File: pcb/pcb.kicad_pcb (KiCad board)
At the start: 2 copper layers, 129 parts, among them J1 Conn_01x06, J2 SPI_Flash, SW1 Select, SW2 Done, U1 ATmega328P-AU, U2 DessinAfficheur, Y1 16Mhz

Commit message: fix i2c label
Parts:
- J1: value Conn_01x06 -> I2C_Data

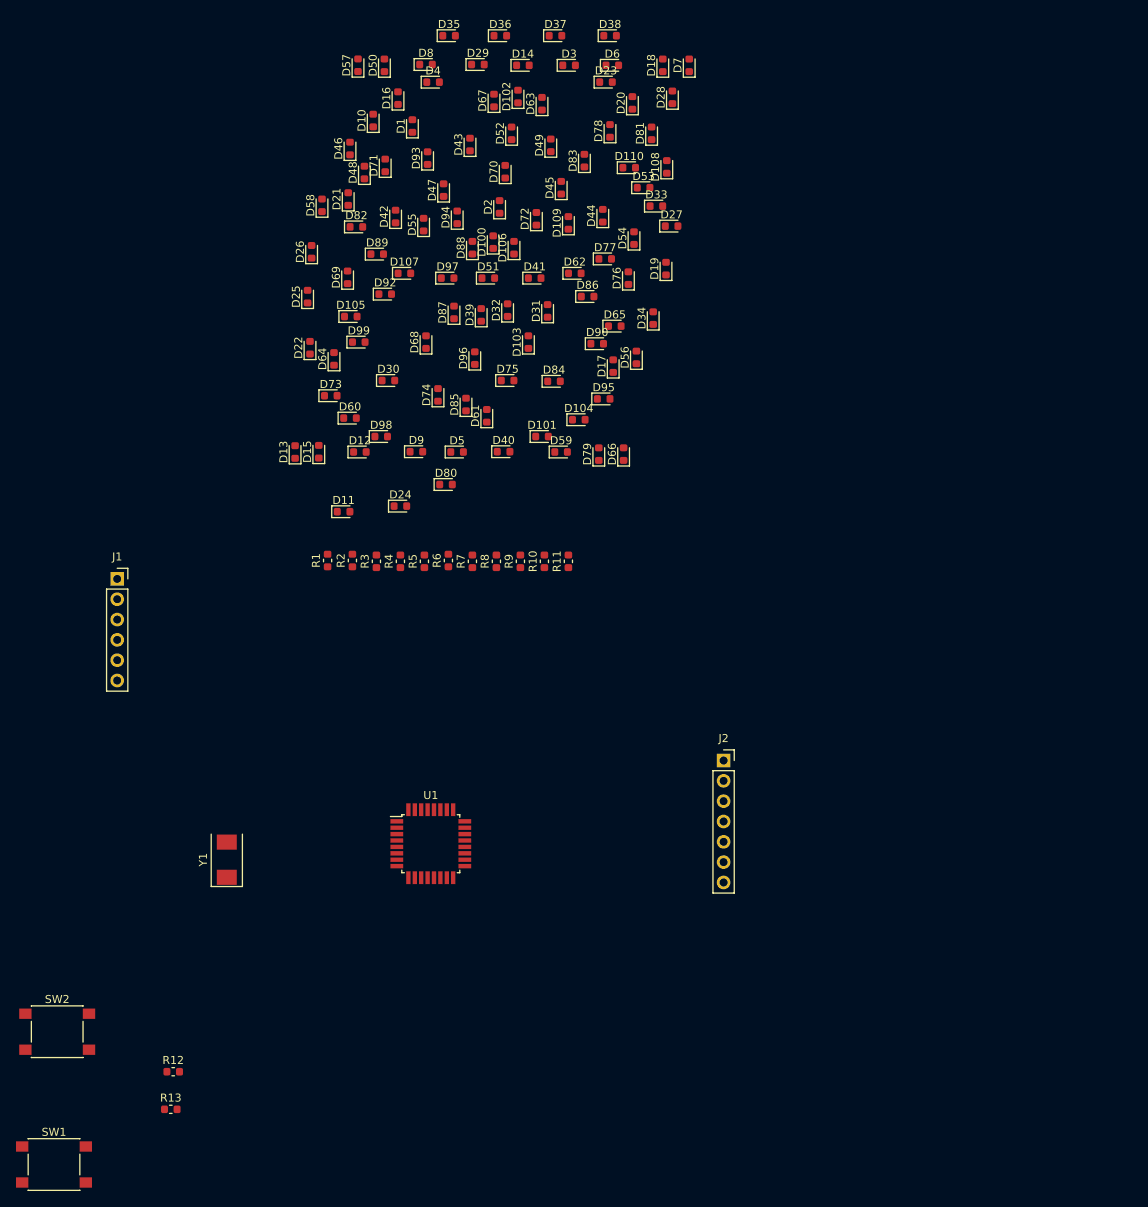
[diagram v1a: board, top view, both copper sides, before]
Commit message: put all components on the board
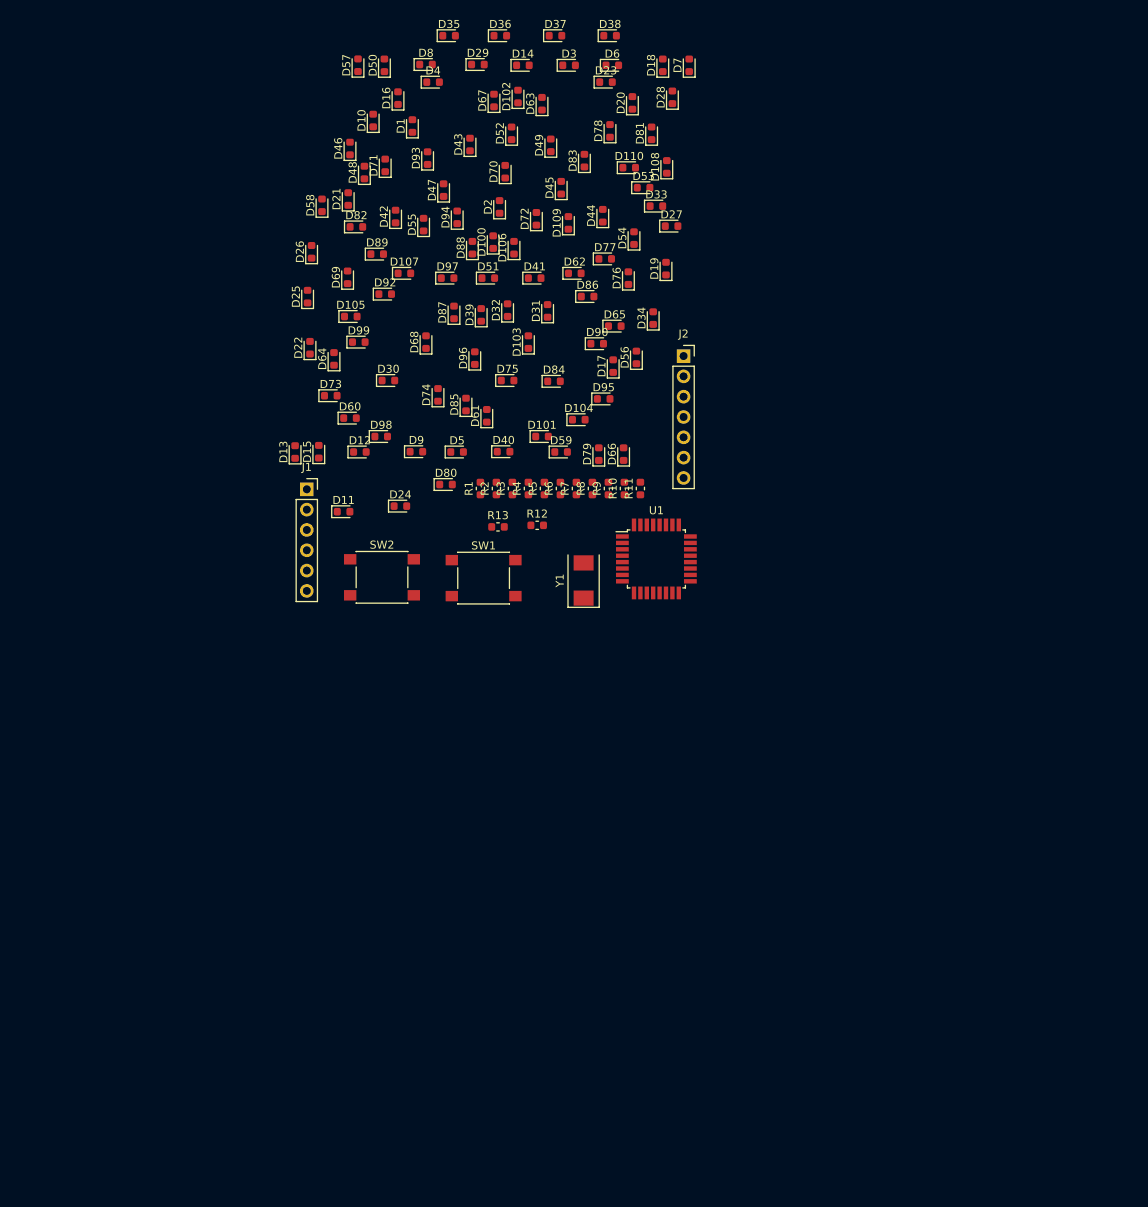
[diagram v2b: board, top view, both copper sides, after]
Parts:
- moved SW1 90.9 mm to (25.2, 68.8)
- moved R13 83.5 mm to (27.0, 62.4)
- moved R12 82.1 mm to (31.9, 62.2)
- moved SW2 69.8 mm to (12.5, 68.7)
- moved Y1 56.6 mm to (37.7, 69.1)
- moved J2 50.8 mm to (50.2, 41.0)
- moved U1 45.4 mm to (46.8, 66.4)
- moved J1 26.2 mm to (3.10, 57.7)
- moved R1 21.1 mm to (24.8, 57.6)
- moved R2 20.1 mm to (26.8, 57.6)
- moved R3 19.3 mm to (28.8, 57.6)
- moved R4 18.4 mm to (30.8, 57.6)
- moved R5 17.5 mm to (32.8, 57.6)
- moved R6 16.6 mm to (34.8, 57.6)
- moved R7 15.9 mm to (36.8, 57.6)
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
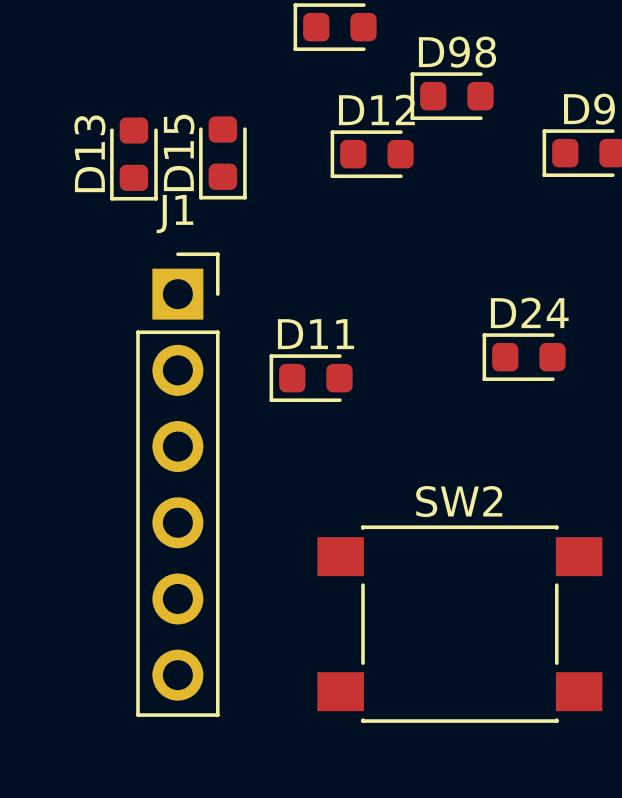
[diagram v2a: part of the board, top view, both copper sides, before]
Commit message: fix gnd of i2c
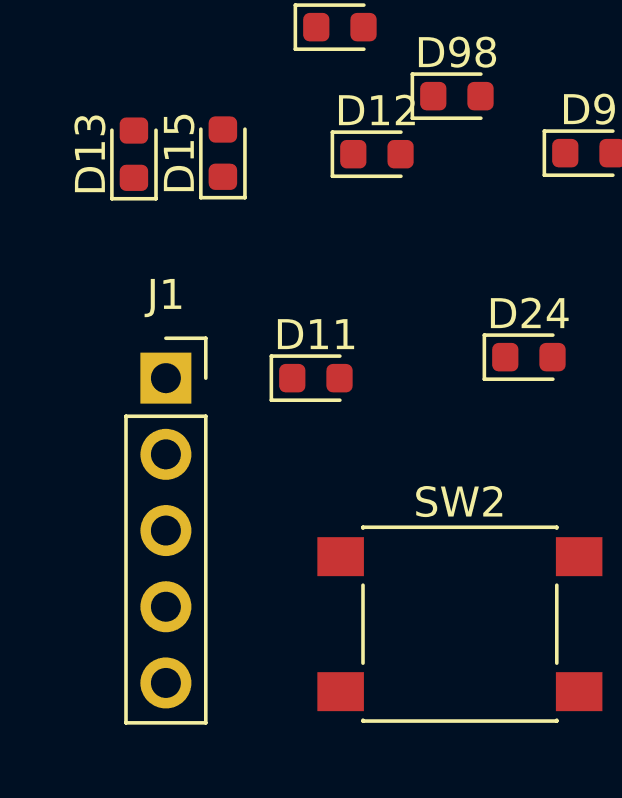
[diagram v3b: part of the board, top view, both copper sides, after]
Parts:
- J1: footprint Connector_PinSocket_2.54mm:PinSocket_1x06_P2.54mm_Vertical -> Connector_PinSocket_2.54mm:PinSocket_1x05_P2.54mm_Vertical
- moved J1 2.83 mm to (2.70, 60.5)
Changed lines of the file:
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@@
     (add_net "Net-(U1-Pad8)")
   )
+  (module Connector_PinSocket_2.54mm:PinSocket_1x05_P2.54mm_Vertical (layer F.Cu)
+    (at 2.7 60.5)
+    (descr "Through hole straight socket strip, 1x05, 2.54mm pitch, single row (from Kicad 4.0.7), script generated")
+    (tags "Through hole socket strip THT 1x05 2.54mm single row")
+    (fp_text reference J1 (at 0 -2.77) (layer F.SilkS)
+      (effects (font (size 1 1) (thickness 0.15)))
+    )
+    (fp_text value I2C_Data (at 0 12.93) (layer F.Fab)
+      (effects (font (size 1 1) (thickness 0.15)))
+    )
+    (fp_text user %R (at 0 5.08 90) (layer F.Fab)
+      (effects (font (size 1 1) (thickness 0.15)))
+    )
+    (fp_line (start -1.27 -1.27) (end 0.635 -1.27) (layer F.Fab) (width 0.1))
+    (fp_line (start 0.635 -1.27) (end 1.27 -0.635) (layer F.Fab) (width 0.1))
+    (fp_line (start 1.27 -0.635) (end 1.27 11.43) (layer F.Fab) (width 0.1))
+    (fp_line (start 1.27 11.43) (end -1.27 11.43) (layer F.Fab) (width 0.1))
+    (fp_line (start -1.27 11.43) (end -1.27 -1.27) (layer F.Fab) (width 0.1))
+    (fp_line (start -1.33 1.27) (end 1.33 1.27) (layer F.SilkS) (width 0.12))
+    (fp_line (start -1.33 1.27) (end -1.33 11.49) (layer F.SilkS) (width 0.12))
+    (fp_line (start -1.33 11.49) (end 1.33 11.49) (layer F.SilkS) (width 0.12))
+    (fp_line (start 1.33 1.27) (end 1.33 11.49) (layer F.SilkS) (width 0.12))
+    (fp_line (start 1.33 -1.33) (end 1.33 0) (layer F.SilkS) (width 0.12))
+    (fp_line (start 0 -1.33) (end 1.33 -1.33) (layer F.SilkS) (width 0.12))
+    (fp_line (start -1.8 -1.8) (end 1.75 -1.8) (layer F.CrtYd) (width 0.05))
+    (fp_line (start 1.75 -1.8) (end 1.75 11.9) (layer F.CrtYd) (width 0.05))
+    (fp_line (start 1.75 11.9) (end -1.8 11.9) (layer F.CrtYd) (width 0.05))
+    (fp_line (start -1.8 11.9) (end -1.8 -1.8) (layer F.CrtYd) (width 0.05))
+    (pad 5 thru_hole oval (at 0 10.16) (size 1.7 1.7) (drill 1) (layers *.Cu *.Mask)
+      (net 12 GND))
+    (pad 4 thru_hole oval (at 0 7.62) (size 1.7 1.7) (drill 1) (layers *.Cu *.Mask)
+      (net 13 "Net-(J1-Pad4)"))
+    (pad 3 thru_hole oval (at 0 5.08) (size 1.7 1.7) (drill 1) (layers *.Cu *.Mask)
+      (net 14 "Net-(J1-Pad3)"))
+    (pad 2 thru_hole oval (at 0 2.54) (size 1.7 1.7) (drill 1) (layers *.Cu *.Mask)
+      (net 15 "Net-(J1-Pad2)"))
+    (pad 1 thru_hole rect (at 0 0) (size 1.7 1.7) (drill 1) (layers *.Cu *.Mask)
+      (net 16 "Net-(J1-Pad1)"))
+    (model ${KISYS3DMOD}/Connector_PinSocket_2.54mm.3dshapes/PinSocket_1x05_P2.54mm_Vertical.wrl
+      (at (xyz 0 0 0))
+      (scale (xyz 1 1 1))
+      (rotate (xyz 0 0 0))
+    )
+  )
   (module Crystal:Crystal_SMD_0603-2Pin_6.0x3.5mm (layer F.Cu)
     (at 37.7 69.1 90)
@@
       (at (xyz 0 0 0))
       (scale (xyz 1 1 1))
-      (rotate (xyz 0 0 0))
-    )
-  )
-  (module Connector_PinSocket_2.54mm:PinSocket_1x06_P2.54mm_Vertical (layer F.Cu)
-    (at 3.1 57.7)
-    (descr "Through hole straight socket strip, 1x06, 2.54mm pitch, single row (from Kicad 4.0.7), script generated")
-    (tags "Through hole socket strip THT 1x06 2.54mm single row")
-    (fp_text reference J1 (at 0 -2.77) (layer F.SilkS)
-      (effects (font (size 1 1) (thickness 0.15)))
-    )
-    (fp_text value I2C_Data (at 0 15.47) (layer F.Fab)
-      (effects (font (size 1 1) (thickness 0.15)))
-    )
-    (fp_line (start -1.27 -1.27) (end 0.635 -1.27) (layer F.Fab) (width 0.1))
-    (fp_line (start 0.635 -1.27) (end 1.27 -0.635) (layer F.Fab) (width 0.1))
-    (fp_line (start 1.27 -0.635) (end 1.27 13.97) (layer F.Fab) (width 0.1))
-    (fp_line (start 1.27 13.97) (end -1.27 13.97) (layer F.Fab) (width 0.1))
-    (fp_line (start -1.27 13.97) (end -1.27 -1.27) (layer F.Fab) (width 0.1))
-    (fp_line (start -1.33 1.27) (end 1.33 1.27) (layer F.SilkS) (width 0.12))
-    (fp_line (start -1.33 1.27) (end -1.33 14.03) (layer F.SilkS) (width 0.12))
-    (fp_line (start -1.33 14.03) (end 1.33 14.03) (layer F.SilkS) (width 0.12))
-    (fp_line (start 1.33 1.27) (end 1.33 14.03) (layer F.SilkS) (width 0.12))
-    (fp_line (start 1.33 -1.33) (end 1.33 0) (layer F.SilkS) (width 0.12))
-    (fp_line (start 0 -1.33) (end 1.33 -1.33) (layer F.SilkS) (width 0.12))
-    (fp_line (start -1.8 -1.8) (end 1.75 -1.8) (layer F.CrtYd) (width 0.05))
-    (fp_line (start 1.75 -1.8) (end 1.75 14.45) (layer F.CrtYd) (width 0.05))
-    (fp_line (start 1.75 14.45) (end -1.8 14.45) (layer F.CrtYd) (width 0.05))
-    (fp_line (start -1.8 14.45) (end -1.8 -1.8) (layer F.CrtYd) (width 0.05))
-    (fp_text user %R (at 0 6.35 90) (layer F.Fab)
-      (effects (font (size 1 1) (thickness 0.15)))
-    )
-    (pad 6 thru_hole oval (at 0 12.7) (size 1.7 1.7) (drill 1) (layers *.Cu *.Mask)
-      (net 12 GND))
-    (pad 5 thru_hole oval (at 0 10.16) (size 1.7 1.7) (drill 1) (layers *.Cu *.Mask)
-      (net 12 GND))
-    (pad 4 thru_hole oval (at 0 7.62) (size 1.7 1.7) (drill 1) (layers *.Cu *.Mask)
-      (net 13 "Net-(J1-Pad4)"))
-    (pad 3 thru_hole oval (at 0 5.08) (size 1.7 1.7) (drill 1) (layers *.Cu *.Mask)
-      (net 14 "Net-(J1-Pad3)"))
-    (pad 2 thru_hole oval (at 0 2.54) (size 1.7 1.7) (drill 1) (layers *.Cu *.Mask)
-      (net 15 "Net-(J1-Pad2)"))
-    (pad 1 thru_hole rect (at 0 0) (size 1.7 1.7) (drill 1) (layers *.Cu *.Mask)
-      (net 16 "Net-(J1-Pad1)"))
-    (model ${KISYS3DMOD}/Connector_PinSocket_2.54mm.3dshapes/PinSocket_1x06_P2.54mm_Vertical.wrl
-      (at (xyz 0 0 0))
-      (scale (xyz 1 1 1))

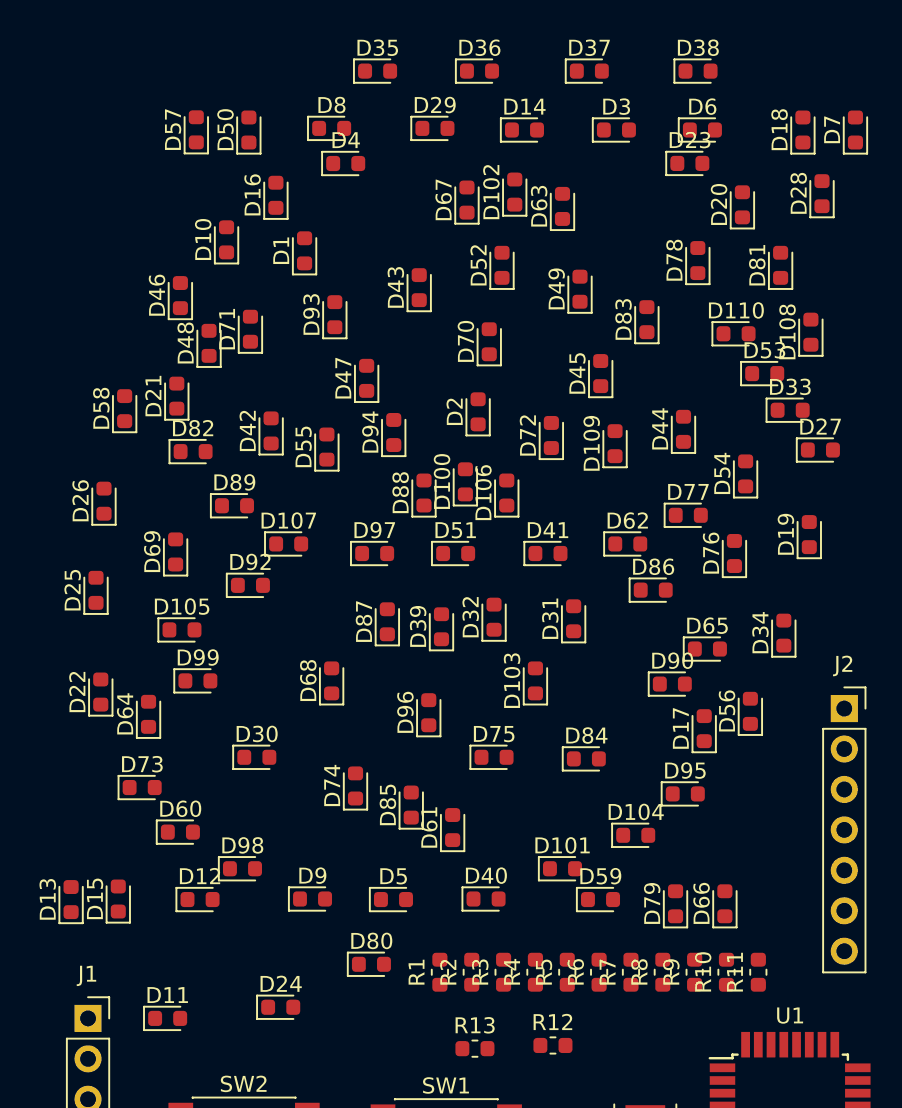
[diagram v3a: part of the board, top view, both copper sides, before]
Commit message: led placement
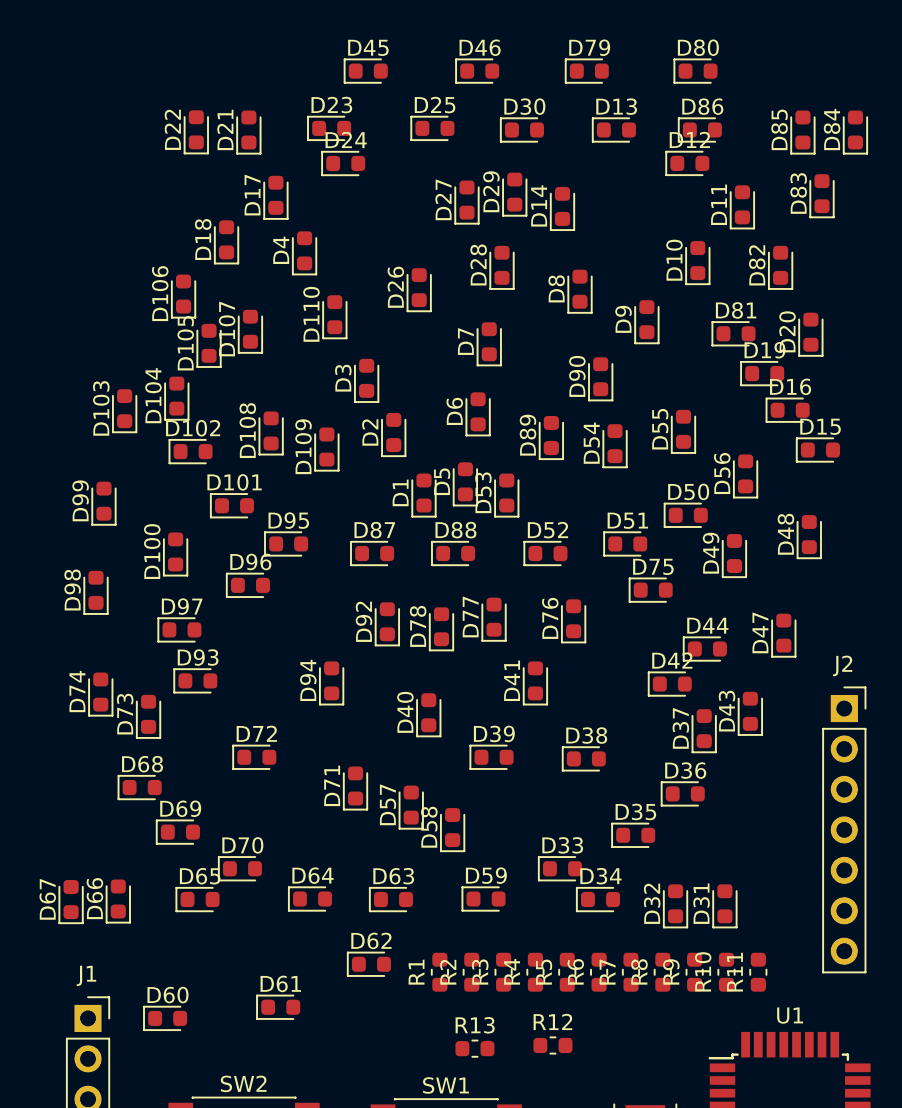
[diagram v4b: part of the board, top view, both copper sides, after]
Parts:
- moved D45 24.0 mm to (20.3, 1.00), turned to 0 degrees
- moved D90 23.8 mm to (34.9, 20.2), turned to 90 degrees
- moved D46 23.5 mm to (27.3, 1.00), turned to 0 degrees
- moved D106 23.3 mm to (8.70, 15.0), turned to 90 degrees
- renumbered D88 to D1, D78 to D10, D69 to D100, D89 to D101, D82 to D102, D58 to D103, D21 to D104, D48 to D105, D36 to D106, D71 to D107, D42 to D108, D55 to D109, D20 to D11, D93 to D110, D23 to D12, D3 to D13, D63 to D14, D27 to D15, D33 to D16, D16 to D17, D10 to D18, D53 to D19, D94 to D2, D108 to D20, D50 to D21, D57 to D22, D8 to D23, D4 to D24, D29 to D25, D43 to D26, D67 to D27, D52 to D28, D102 to D29, D47 to D3, D14 to D30, D66 to D31, D79 to D32, D101 to D33, D59 to D34, D104 to D35, D95 to D36, D17 to D37, D84 to D38, D75 to D39, D1 to D4, D96 to D40, D103 to D41, D90 to D42, D56 to D43, D65 to D44, D34 to D47, D19 to D48, D76 to D49, D100 to D5, D77 to D50, D62 to D51, D41 to D52, D106 to D53, D109 to D54, D44 to D55, D54 to D56, D85 to D57, D61 to D58, D40 to D59, D2 to D6, D11 to D60, D24 to D61, D80 to D62, D5 to D63, D9 to D64, D12 to D65, D15 to D66, D13 to D67, D73 to D68, D60 to D69, D70 to D7, D98 to D70, D74 to D71, D30 to D72, D64 to D73, D22 to D74, D86 to D75, D31 to D76, D32 to D77, D39 to D78, D37 to D79, D49 to D8, D38 to D80, D110 to D81, D81 to D82, D28 to D83, D7 to D84, D18 to D85, D6 to D86, D97 to D87, D51 to D88, D72 to D89, D83 to D9, D35 to D90, D87 to D92, D99 to D93, D68 to D94, D107 to D95, D92 to D96, D105 to D97, D25 to D98, D26 to D99
